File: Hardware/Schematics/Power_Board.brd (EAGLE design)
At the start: 99 x 48.5 mm, 64 parts, among them IC3 74AC373DW, J1 1X2-3.5MM, J2 1X2-3.5MM, J4 1X2-3.5MM, Q1 BSL207SP, Q2 BSL207SP, Q3 MOSFET-NCHANNELSMD, Q8 4.096MHz, U1 ESP-32S

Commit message: Created new logicboard with isolation from HV side.
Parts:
- removed BUTTON1, BUTTON2, BUTTON3: (no value), pinhead:1X03
- removed C1, C17, C18, C2, C3, C4, C5, C6, C7: 100nF, rcl:C1206
- removed FLASH, RESET: -, switch-omron:B3F-10XX
- removed IC3: 74AC373DW, 74xx-eu:SO20W
- removed J1: 1X2-3.5MM, adafruit:1X2-3.5MM
- removed JTAG, UART: -, pinhead:1X04
- removed Q4, Q5, Q6: (no value), adafruit:SOT23
- removed R1, R17, R2: 10K, rcl:R0805
- removed R20, R22, R7: 100, rcl:R0805
- removed U$11, U$4, U$6, U$7: ADUM1410, PowerSocket:SOIC-16
- removed U$8: HLK-PM03, PowerSocket:HLK-PM03
- removed U1: ESP-32S, esp32:ESP-32S
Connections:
- removed net BUTTON1: BUTTON1.3, U1.33
- removed net BUTTON2: BUTTON2.3, U1.30
- removed net BUTTON3: BUTTON3.3, U1.28
- removed net CS2: U$7.14
- removed net CS3: U$11.11
- removed net FLASH: FLASH.3, FLASH.4, R2.2, U1.25
- removed net GND: C1.2, C17.2, C2.2, C4.2, C7.2, FLASH.1, FLASH.2, IC3.1, IC3.10, IC3.13, IC3.14, IC3.17, IC3.18, IC3.8, Q4.2, Q5.2, Q6.2, R17.2, RESET.1, RESET.2, U$11.2, U$11.7, U$11.8, U$4.2, U$4.7, U$4.8, U$6.15, U$6.9, U$7.2, U$7.7, U$7.8, U$8.-VO, U1.1, U1.15, U1.24, U1.38, U1.GND, UART.1
- removed net LED1: Q5.1, U1.31
- removed net LED1_SWITCHED: Q5.3, R7.2
- removed net LED2: Q4.1, U1.29
- removed net LED2_SWITCHED: Q4.3, R20.2
- removed net LED3: Q6.1, U1.27
- removed net LED3_SWITCHED: Q6.3, R22.2
- removed net N$1: J1.2, U$8.AC1
- removed net N$11: BUTTON3.2, R22.1
- removed net N$13: J1.1, U$8.AC2
- removed net N$14: U$6.7, U$6.8
- removed net N$2: JTAG.1, U1.23
- removed net N$24: U$6.6
- removed net N$27: U$6.5
- removed net N$28: U$6.4
- removed net N$29: U$6.14
- removed net N$3: JTAG.2, U1.16
- removed net N$31: U$6.13
- removed net N$32: IC3.11, R17.1, U1.9
- removed net N$33: IC3.3, U1.12
- removed net N$34: IC3.4, U1.11
- removed net N$35: IC3.7, U1.10
- removed net N$36: U$6.12
- removed net N$37: U$6.11
- removed net N$39: U$6.10
- removed net N$4: JTAG.3, U1.14
- removed net N$40: U$4.6
- removed net N$41: U$4.5
- removed net N$45: U$4.4
- removed net N$49: U$4.3
- removed net N$5: JTAG.4, U1.13
- removed net N$51: U$7.3
- removed net N$52: U$7.4
- removed net N$53: U$7.5
- removed net N$54: U$11.6, U$7.6
- removed net N$55: U$11.5
- removed net N$66: R1.1, RESET.3, RESET.4, U1.3
- removed net N$7: BUTTON2.2, R20.1
- removed net N$70: U1.35, UART.2
- removed net N$77: U1.34, UART.3
- removed net N$9: BUTTON1.2, R7.1
- removed net RELAY1: U$4.13
- removed net RELAY2: U$4.12
- removed net RELAY3: U$4.11
- removed net VCC: BUTTON1.1, BUTTON2.1, BUTTON3.1, C1.1, C17.1, C2.1, C4.1, C7.1, IC3.20, R1.2, R2.1, U$11.1, U$4.1, U$6.16, U$7.1, U$8.+VO, U1.2, UART.4
- net +5V: no longer C18.1, C3.1, C5.1, C6.1, U$11.16, U$4.16, U$6.1, U$7.16
- net CS1: no longer U$7.13
- net GND1: no longer C18.2, C3.2, C5.2, C6.2, U$11.15, U$11.9, U$4.15, U$4.9, U$6.2, U$7.15, U$7.9
- net RELAY_SUPL_CTRL: no longer U$4.14
- net RESET: no longer U$11.12
- net SCLK: no longer U$7.12
- net SDI: no longer U$7.11
- net SDO: no longer U$6.3

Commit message: Power board schematic mostly done.
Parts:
- added C1, C19, C2, C20, C21, C3: 100nF, rcl:C1206
- added C17, C22, C23, C25, C26, C4, C5, C7: 220nF, rcl:C1206
- added C18, C24, C27, C6: 22nF, rcl:C1206
- added C28: (no value), rcl:E3,5-8
- added D1, D2: (no value), diode:DO-214AC
- added J1, J3: 1X2-3.5MM, adafruit:1X2-3.5MM
- added Q4, Q6: (no value), adafruit:SOT23
- added Q5, Q9: 4.096MHz, crystal:HC49U70
- added R1: 1K, resistor:R0805
- added R11, R13, R14, R17, R19, R20: 1K, rcl:R0805
- added R12, R18: 12m, rcl:R2512
- added R15, R2: 1M, rcl:R0805
- added R16, R7: 560, rcl:R1206
- added U$10, U$15: POWER_SOCKET_EU, PowerSocket:POWER_SOCKET_EU
- added U$11, U$13, U$6, U$7: RELAYPTH, SRD-05VDC-SL-C:SRD-05VDC-SL-C
- added U$14, U$8: CS5463, PowerSocket:SO24L
- added U$4: PCF8574AT, i2c:SO16
- JP1: device pinhead:2X16/90 -> pinhead:2X09/90
- moved C10 556.3 mm to (-93.7, 238.7)
- moved C11 556.3 mm to (-93.7, 182.3)
- moved C12 556.3 mm to (-93.7, 176.2)
- moved C13 556.3 mm to (-93.7, 151.3)
- moved C8 556.3 mm to (-93.7, 250.9)
- moved C9 556.3 mm to (-93.7, 244.8)
- moved J2 556.3 mm to (-83.5, 104.1)
- moved Q8 556.3 mm to (-87.1, 260.6)
- moved R10 556.3 mm to (-94.2, 118.1)
- moved R5 556.3 mm to (-45.0, 188.4)
- moved R8 556.3 mm to (-46.4, 132.5)
- moved R9 556.3 mm to (-94.2, 124.2)
- moved U$9 556.3 mm to (-6.20, 291.7)
- moved R4 556.3 mm to (-44.5, 201.1)
- moved R6 556.3 mm to (-44.5, 157.4)
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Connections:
- removed net +5V: C10.1, C9.1, Q2.4, R3.2, U$1.P$2, U$5.+VO, U$9.14, U$9.3
- removed net GND1: C10.2, C11.2, C12.1, C14.2, C15.1, C8.2, C9.2, Q3.2, Q7.2, U$1.P$1, U$1.P$4, U$5.-VO, U$9.13, U$9.4, U$9.8
- new net AC1: J4.1, U$5.AC1
- new net AC2: J4.2, U$5.AC2
- new net CS2: JP1.14, U$8.7
- new net CS3: JP1.15, U$14.7
- new net GND: C1.2, C10.2, C11.2, C12.1, C14.2, C15.1, C17.1, C19.2, C2.2, C20.2, C21.2, C22.2, C23.1, C25.2, C26.1, C28.-, C3.2, C4.2, C5.1, C7.2, C8.2, C9.2, JP1.1, JP1.10, JP1.13, JP1.18, JP1.6, Q3.2, Q4.2, Q6.2, Q7.2, U$1.P$1, U$1.P$4, U$14.13, U$14.4, U$14.8, U$4.1, U$4.2, U$4.3, U$4.8, U$5.-VO, U$8.13, U$8.4, U$8.8, U$9.13, U$9.4, U$9.8
- new net INT1: U$4.10, U$9.20
- new net INT2: U$4.11, U$8.20
- new net INT3: U$14.20, U$4.12
- new net N$1: D1.A, Q4.3, U$6.COIL0, U$7.COIL0
- new net N$11: C19.1, U$14.11, U$14.12
- new net N$13: C25.1, C27.1, R20.2, U$14.16
- new net N$14: Q9.2, U$14.24
- new net N$19: R16.2, R17.1, R18.1, R20.1, U$11.SWCOMMON
- new net N$2: Q5.1, U$8.1
- new net N$24: C26.2, C27.2, R19.2, U$14.15
- new net N$3: C1.1, U$8.11, U$8.12
- new net N$4: C18.1, C7.1, R14.2, U$8.16
- new net N$5: Q5.2, U$8.24
- new net N$7: C17.2, C18.2, R13.2, U$8.15
- new net N$9: Q9.1, U$14.1
- new net NULL2: J1.1, R2.1, U$7.SWCOMMON
- new net NULL2_OUT: U$10.AC1, U$7.SWCLOSED
- new net NULL3: J3.1, R15.1, U$13.SWCOMMON
- new net NULL3_OUT: U$13.SWCLOSED, U$15.AC1
- new net PC8574_INT: JP1.3, R1.1, U$4.13
- new net PHASE2: J1.2, R12.2, R13.1
- new net PHASE2_OUT: U$10.AC2, U$6.SWCLOSED
- new net PHASE3: J3.2, R18.2, R19.1
- new net PHASE3_OUT: U$11.SWCLOSED, U$15.AC2
- new net RELAY1: Q7.1, U$4.5
- new net RELAY2: Q4.1, U$4.6
- new net RELAY3: Q6.1, U$4.7
- new net SCL: JP1.5, U$4.14
- new net SDA: JP1.8, U$4.15
- new net VCC: C10.1, C2.1, C20.1, C21.1, C28.+, C3.1, C9.1, JP1.16, JP1.17, JP1.2, JP1.7, Q2.4, R1.2, R3.2, U$1.P$2, U$14.14, U$14.3, U$4.16, U$5.+VO, U$8.14, U$8.3, U$9.14, U$9.3
- new net VIN+2: C5.2, C6.2, R2.2, R7.1, U$8.9
- new net VIN+3: C23.2, C24.2, R15.2, R16.1, U$14.9
- new net VIN-2: C4.1, C6.1, R11.2, U$8.10
- new net VIN-3: C22.1, C24.1, R17.2, U$14.10
- net CS1: now also JP1.11
- net N$6: now also R11.1, R12.1, R14.1, R7.2, U$6.SWCOMMON; no longer J4.2, U$5.AC1
- net N$8: now also D2.A, Q6.3, U$11.COIL0, U$13.COIL0; no longer J4.1, U$5.AC2
- net RELAY_SUPL_CTRL: now also U$4.4
- net RELAY_SUPPLY: now also D1.C, D2.C, U$11.COIL1, U$13.COIL1, U$6.COIL1, U$7.COIL1
- net RESET: now also U$14.19, U$4.9, U$8.19
- net SCLK: now also JP1.12, U$14.5, U$8.5
- net SDI: now also JP1.9, U$14.23, U$8.23
- net SDO: now also JP1.4, U$14.6, U$8.6
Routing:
- net AC1: track 0.00 -> 22.4 mm
- net AC2: track 0.00 -> 11.2 mm
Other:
- board size 99 x 48.5 mm -> 149.5 x 49 mm

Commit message: Relay board placement mostly done. Routing ~50% done.
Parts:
- added C29: 100nF, rcl:C0805
- C1, C10, C11, C12, C13, C14, C15, C16, C17, C18, C19, C2, C20, C21, C22, C23, C24, C25, C26, C27, C3, C4, C5, C6, C7, C8, C9: device rcl:C1206 -> rcl:C0805
- C28: device rcl:E3,5-8 -> rcl:E5-6
- Q1, Q2: value BSL207SP -> MOSFET-PCHANNEL_SOT23-3; device transistor-fet:SC74_INFINEON -> Simplex-DiscreteSemi:SOT23-3
- U$10, U$12, U$15: device PowerSocket:POWER_SOCKET_EU -> PowerSocket:POWER_SOCKET_EU_PLATED_THROUGH
- U$11, U$13, U$2, U$3, U$6, U$7: device SRD-05VDC-SL-C:SRD-05VDC-SL-C -> PowerSocket:SRD-05VDC-SL-C
- moved C28 487.6 mm to (145.6, 3.90), turned to 180 degrees
- moved D4 415.5 mm to (114.2, 36.0), flipped to the bottom
- moved Q7 408.4 mm to (113.3, 30.5), flipped to the bottom
- moved R3 381.9 mm to (57.0, 10.2)
- moved Q3 377.9 mm to (52.6, 11.1)
- moved Q2 376.7 mm to (55.9, 12.8), turned to 90 degrees
- moved Q1 370.5 mm to (49.7, 12.6), turned to 270 degrees
- moved U$1 361.9 mm to (54.6, 7.40), turned to 180 degrees
- moved Q8 326.9 mm to (114.5, 3.30)
- moved C8 309.6 mm to (107.0, 15.1), flipped to the bottom, turned to 270 degrees
- moved C9 308.4 mm to (118.4, 20.9), flipped to the bottom, turned to 180 degrees
- moved C10 305.6 mm to (106.7, 8.00), flipped to the bottom, turned to 90 degrees
- moved U$9 304.5 mm to (114.4, 12.1), flipped to the bottom, turned to 90 degrees
- moved C11 244.7 mm to (107.5, 43.1), flipped to the bottom
- moved C12 238.5 mm to (106.3, 46.2), flipped to the bottom, turned to 90 degrees
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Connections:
- removed net AC1: J4.1, U$5.AC1
- removed net AC2: J4.2, U$5.AC2
- new net NULL_PS: J4.1, U$5.AC2
- net 1.8V: now also Q1.2, U$1.2; no longer Q1.4, U$1.P$3
- net GND: now also C29.1, U$1.3, U$1.4; no longer U$1.P$1, U$1.P$4
- net N$10: now also Q1.1; no longer Q1.3
- net N$19: now also U$11.SWOPEN; no longer U$11.SWCOMMON
- net N$26: now also U$3.SWOPEN; no longer U$2.SWCOMMON
- net N$6: now also U$6.SWOPEN; no longer U$6.SWCOMMON
- net NULL1: now also U$2.SWOPEN; no longer U$3.SWCOMMON
- net NULL1_OUT: now also U$12.P$1, U$2.SWCOMMON; no longer U$12.AC1, U$3.SWCLOSED
- net NULL2: now also U$7.SWOPEN; no longer U$7.SWCOMMON
- net NULL2_OUT: now also U$10.P$1, U$7.SWCOMMON; no longer U$10.AC1, U$7.SWCLOSED
- net NULL3: now also U$13.SWOPEN; no longer U$13.SWCOMMON
- net NULL3_OUT: now also U$13.SWCOMMON, U$15.P$1; no longer U$13.SWCLOSED, U$15.AC1
- net PHASE1: now also J4.2, U$5.AC1; no longer J2.2
- net PHASE1_OUT: now also U$12.P$3, U$3.SWCOMMON; no longer U$12.AC2, U$2.SWCLOSED
- net PHASE2: now also J2.2; no longer J1.2
- net PHASE2_OUT: now also U$10.P$3, U$6.SWCOMMON; no longer U$10.AC2, U$6.SWCLOSED
- net PHASE3: now also J1.2; no longer J3.2
- net PHASE3_OUT: now also U$11.SWCOMMON, U$15.P$3; no longer U$11.SWCLOSED, U$15.AC2
- net RELAY_SUPL_CTRL: now also Q2.1; no longer Q2.3
- net RELAY_SUPPLY: now also Q1.3, Q2.3; no longer Q1.1, Q1.2, Q1.5, Q1.6, Q2.1, Q2.2, Q2.5, Q2.6
- net VCC: now also C29.2, Q2.2, U$1.1; no longer Q2.4, U$1.P$2
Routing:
- net RELAY_SUPPLY: track 0.00 -> 144.6 mm
- net VCC: track 0.00 -> 39.1 mm
- net AC1: track 22.4 -> 0.00 mm
- net RELAY_SUPL_CTRL: track 0.00 -> 17.1 mm, vias 0 -> 1
- net PHASE1: track 0.00 -> 15.4 mm
- net VIN+3: track 0.00 -> 13.5 mm
- net AC2: track 11.2 -> 0.00 mm
- net NULL3: track 0.00 -> 10.4 mm
- net GND: track 0.00 -> 10.4 mm
- net PC8574_INT: track 0.00 -> 10.3 mm
- net N$10: track 0.00 -> 9.50 mm
- net PHASE2: track 0.00 -> 6.80 mm
- net PHASE3: track 0.00 -> 6.60 mm
- net N$19: track 0.00 -> 6.55 mm, vias 0 -> 5
- net NULL_PS: track 0.00 -> 5.89 mm
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- added copper zone on layer 1, net GND
- added copper zone on layer 16, net GND
- added copper zone on layer 1, net N$19
- added copper zone on layer 16, net N$19
- added copper zone on layer 1, net N$26
- added copper zone on layer 16, net N$26
- added copper zone on layer 1, net N$6
- added copper zone on layer 16, net N$6
- added copper zone on layer 1, net NULL1
- added copper zone on layer 16, net NULL1
- added copper zone on layer 1, net NULL1_OUT
- added copper zone on layer 16, net NULL1_OUT
- added copper zone on layer 1, net NULL2
- added copper zone on layer 16, net NULL2
- added copper zone on layer 1, net NULL2_OUT
- added copper zone on layer 16, net NULL2_OUT
- added copper zone on layer 1, net NULL3_OUT
- added copper zone on layer 16, net NULL3_OUT
- added copper zone on layer 16, net PHASE1
- added copper zone on layer 1, net PHASE1_OUT
- added copper zone on layer 16, net PHASE1_OUT
- added copper zone on layer 1, net PHASE2_OUT
- added copper zone on layer 16, net PHASE2_OUT
- added copper zone on layer 1, net PHASE3_OUT
- added copper zone on layer 16, net PHASE3_OUT
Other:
- board size 149.5 x 49 mm -> 139.3 x 49 mm

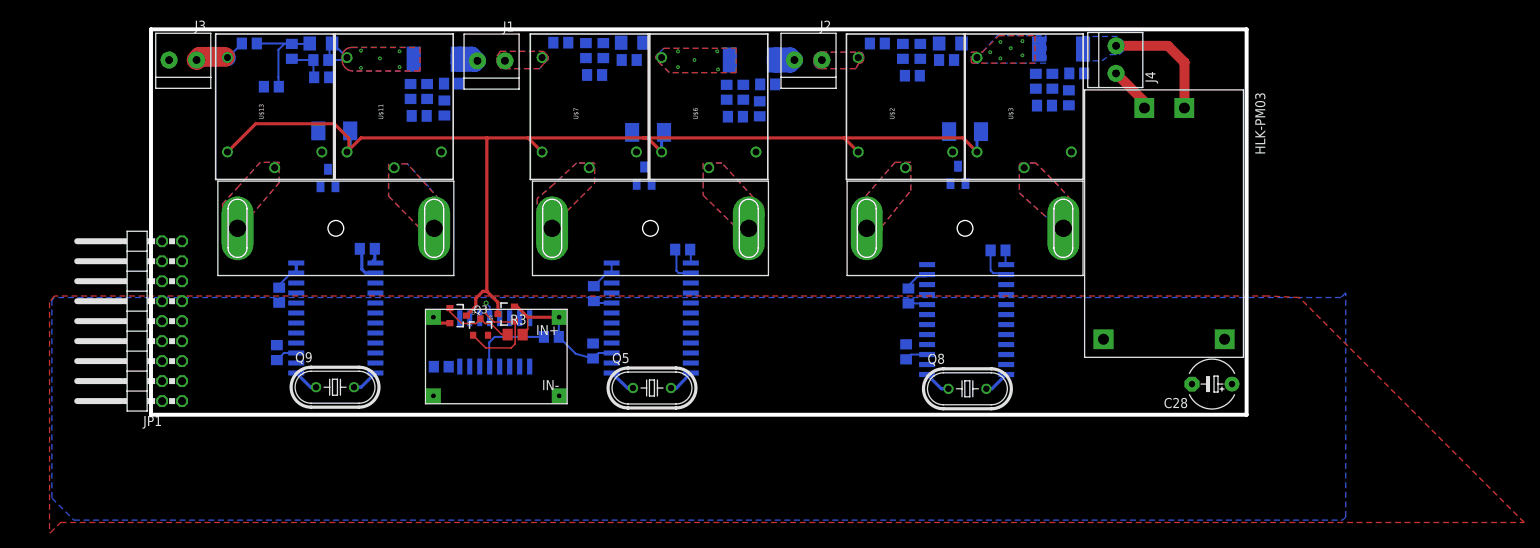
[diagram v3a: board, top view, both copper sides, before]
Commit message: Power board routing done. Still missing adjustments of soldermask and silkscreen on both powerboard and logic board.
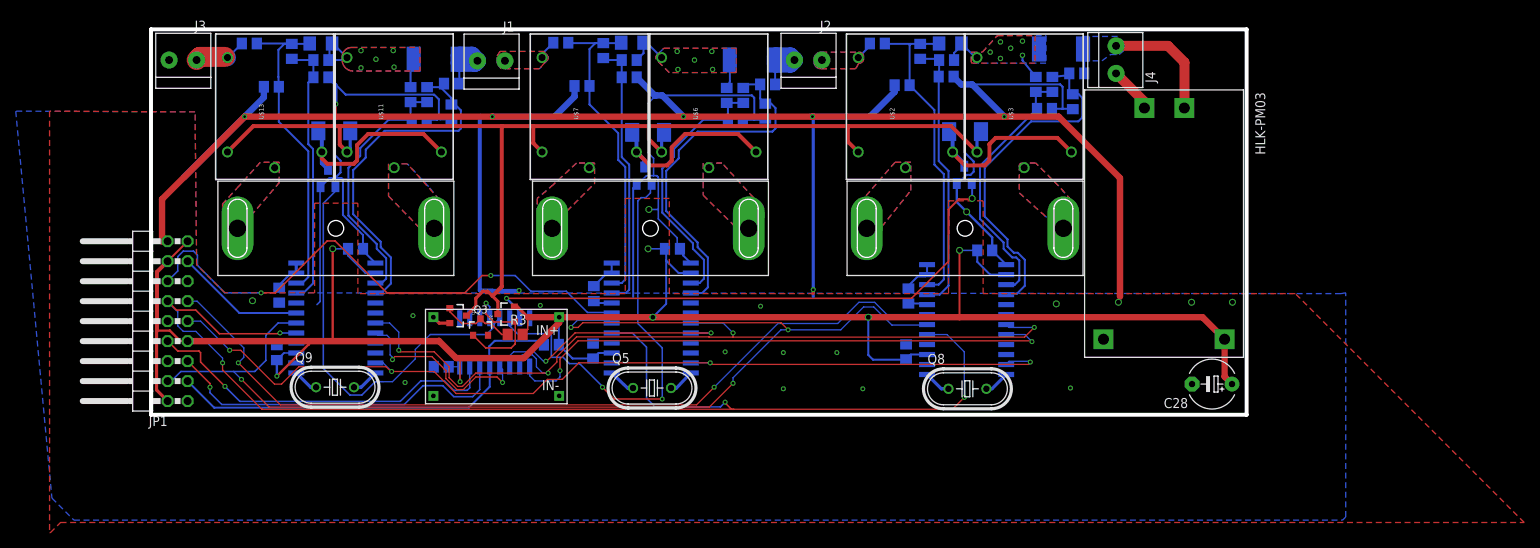
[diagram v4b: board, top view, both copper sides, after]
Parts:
- R1: value 1K -> 2.5K
- moved C5 4.53 mm to (65.5, 41.8), turned to 180 degrees
- moved C4 4.41 mm to (71.5, 42.9), turned to 180 degrees
- moved C12 4.30 mm to (106.2, 41.9), turned to 180 degrees
- moved C11 4.30 mm to (111.8, 43.0), turned to 180 degrees
- moved C9 1.70 mm to (116.7, 20.9)
- moved C21 1.50 mm to (36.7, 21.1)
- moved C3 1.30 mm to (77.0, 21.1)
- moved C26 1.03 mm to (48.9, 38.5)
- moved R1 1.00 mm to (61.6, 8.90)
- moved Q7 0.80 mm to (114.1, 30.5)
- moved C17 0.76 mm to (88.8, 38.6)
- moved C15 0.71 mm to (127.9, 39.8)
- moved JP1 0.70 mm to (9.00, 11.9)
- moved C25 0.50 mm to (44.8, 37.5)
- moved C14 0.40 mm to (124.3, 38.9)
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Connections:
- net INT1: now also U$4.9; no longer U$4.10
- net N$13: now also U$14.15; no longer U$14.16
- net N$24: now also U$14.16; no longer U$14.15
- net N$30: now also U$9.16; no longer U$9.15
- net N$4: now also U$8.15; no longer U$8.16
- net N$42: now also U$9.15; no longer U$9.16
- net N$7: now also U$8.16; no longer U$8.15
- net RELAY1: now also U$4.7; no longer U$4.5
- net RELAY3: now also U$4.5; no longer U$4.7
- net RESET: now also U$4.10; no longer U$4.9
- net VIN+1: now also U$9.10; no longer U$9.9
- net VIN+2: now also U$8.10; no longer U$8.9
- net VIN+3: now also U$14.10; no longer U$14.9
- net VIN-1: now also U$9.9; no longer U$9.10
- net VIN-2: now also U$8.9; no longer U$8.10
- net VIN-3: now also U$14.9; no longer U$14.10
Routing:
- net GND: track 10.4 -> 447.6 mm, vias 0 -> 25
- net VCC: track 39.1 -> 289.9 mm, vias 0 -> 7
- net SCLK: track 0.00 -> 163.1 mm, vias 0 -> 4
- net SDO: track 0.00 -> 152.3 mm, vias 0 -> 4
- net SDI: track 0.00 -> 123.1 mm, vias 0 -> 4
- net RESET: track 0.00 -> 109.6 mm, vias 0 -> 4
- net CS1: track 0.00 -> 107.6 mm, vias 0 -> 2
- net RELAY1: track 0.00 -> 73.7 mm, vias 0 -> 2
- net INT1: track 0.00 -> 73.3 mm, vias 0 -> 2
- net CS2: track 0.00 -> 70.6 mm, vias 0 -> 2
- net RELAY2: track 0.00 -> 55.6 mm, vias 0 -> 2
- net RELAY3: track 0.00 -> 53.2 mm
- net SDA: track 0.00 -> 46.7 mm, vias 0 -> 1
- net N$7: track 0.00 -> 45.6 mm
- net SCL: track 0.00 -> 45.2 mm, vias 0 -> 1
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
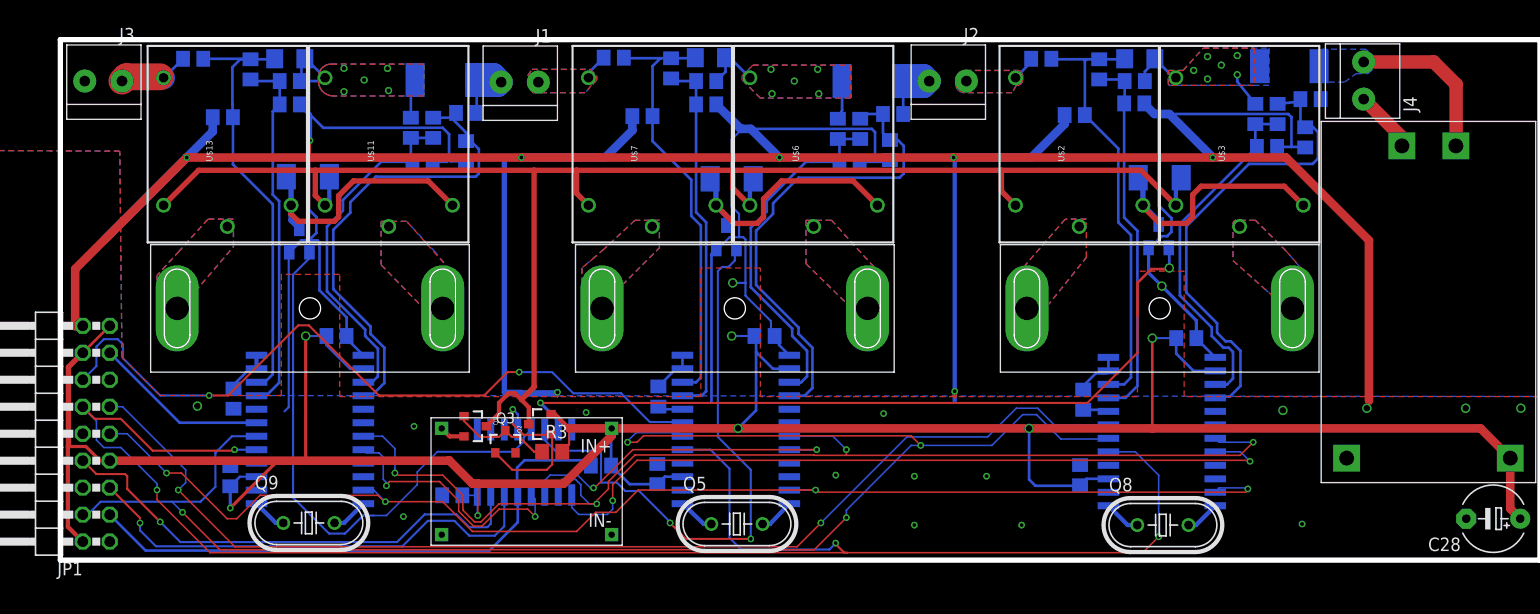
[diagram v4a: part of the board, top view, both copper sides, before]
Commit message: Values and names fixed in silkscreen for powerboard. Slots added to powerboard.
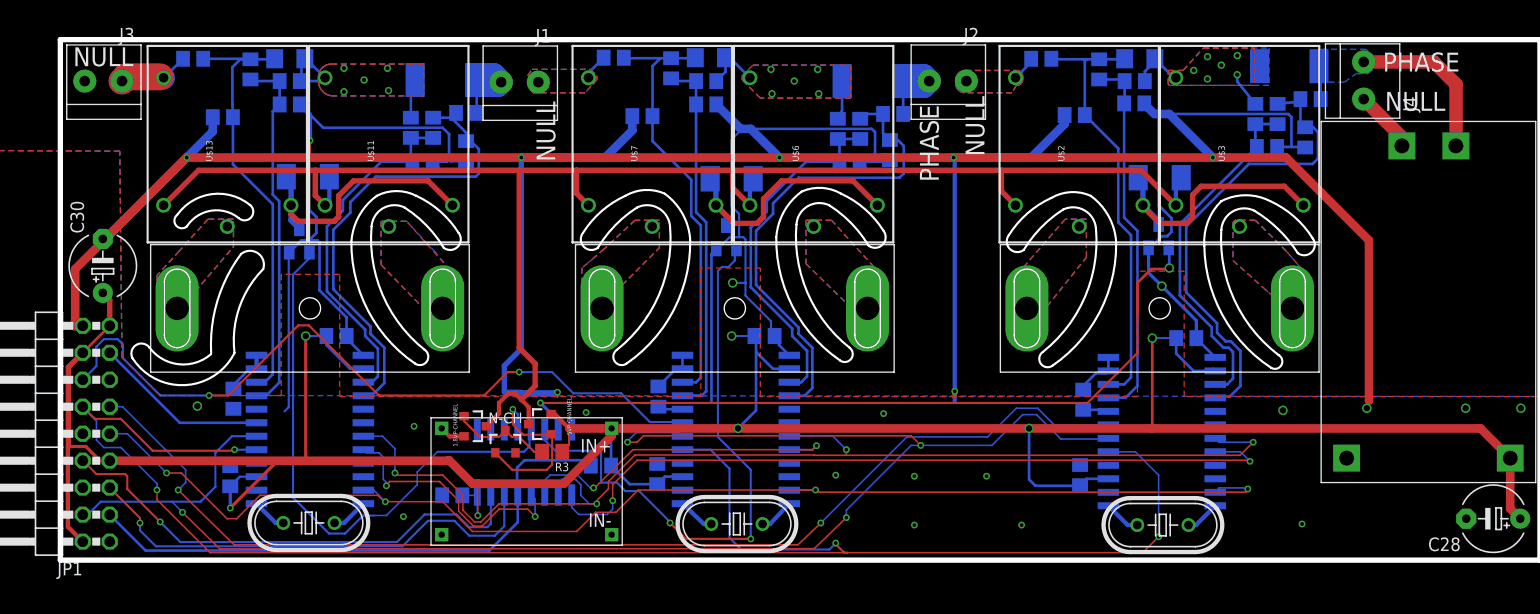
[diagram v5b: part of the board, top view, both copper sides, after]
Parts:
- added C30: 100µF, rcl:E5-6
- C28: value (none) -> 100µF
- renumbered Q1 to 1.8VP-CHANNEL, Q2 to 5VP-CHANNEL, Q3 to N-CH
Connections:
- net GND: now also C30.-
- net VCC: now also C30.+
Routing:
- net VCC: track 289.9 -> 293.3 mm
- net RELAY_SUPPLY: track 151.6 -> 152.3 mm
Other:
- outline, holes or cut-outs redrawn
- board text added: "NULL"
- board text added: "PHASE"

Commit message: Made Logic Board a bit smaller.
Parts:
- added R21: S14K11, varistor:S14K11
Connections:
- net NULL_PS: now also R21.2
- net PHASE1: now also R21.1
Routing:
- net PHASE1: track 18.5 -> 23.9 mm
- net NULL_PS: track 5.89 -> 8.81 mm
